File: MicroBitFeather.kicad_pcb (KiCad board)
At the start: 2 copper layers, 16 parts, among them J1 Feather_Long, J2 Barrel_Jack_MountingPin, J3 Feather_Short, J4 NeoPixels, J5 microbit_edge_connector, U1 74AHCT125, U2 MCP1702-3302E_TO92

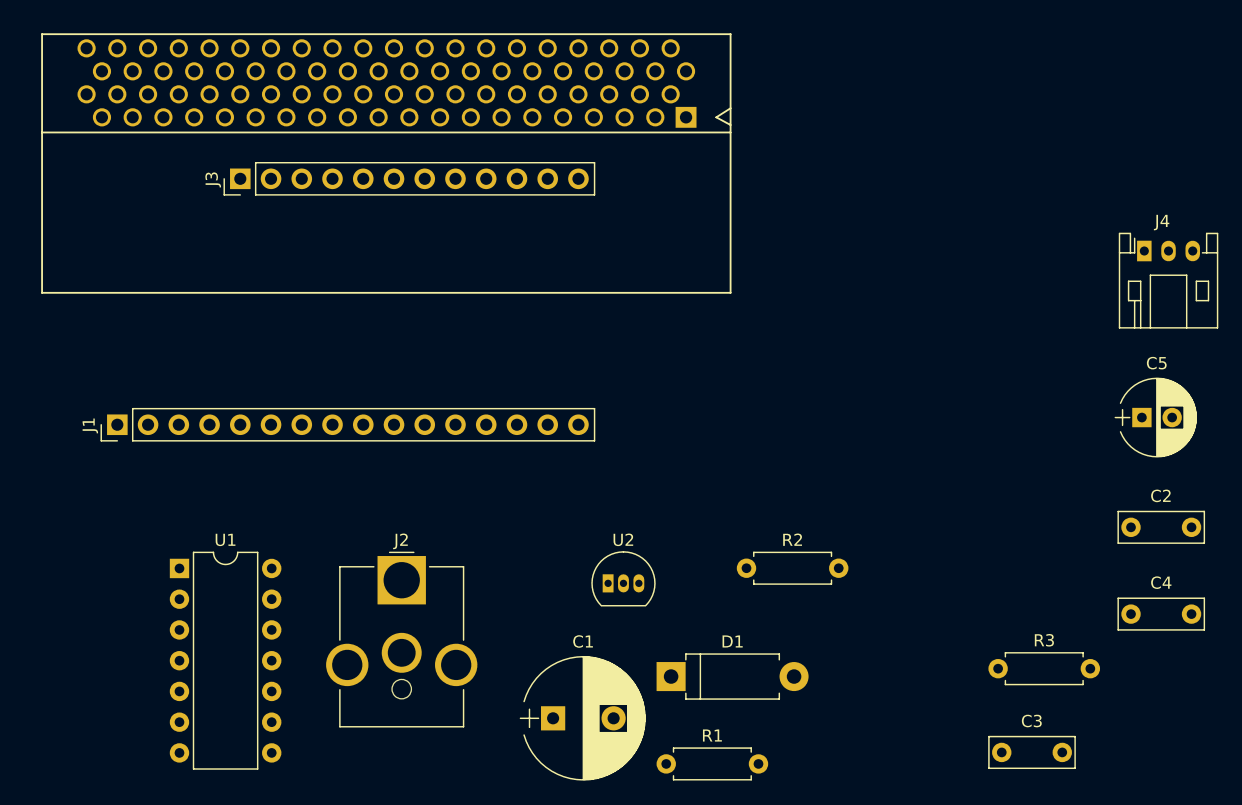
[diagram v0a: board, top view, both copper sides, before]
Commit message: Place footprints.
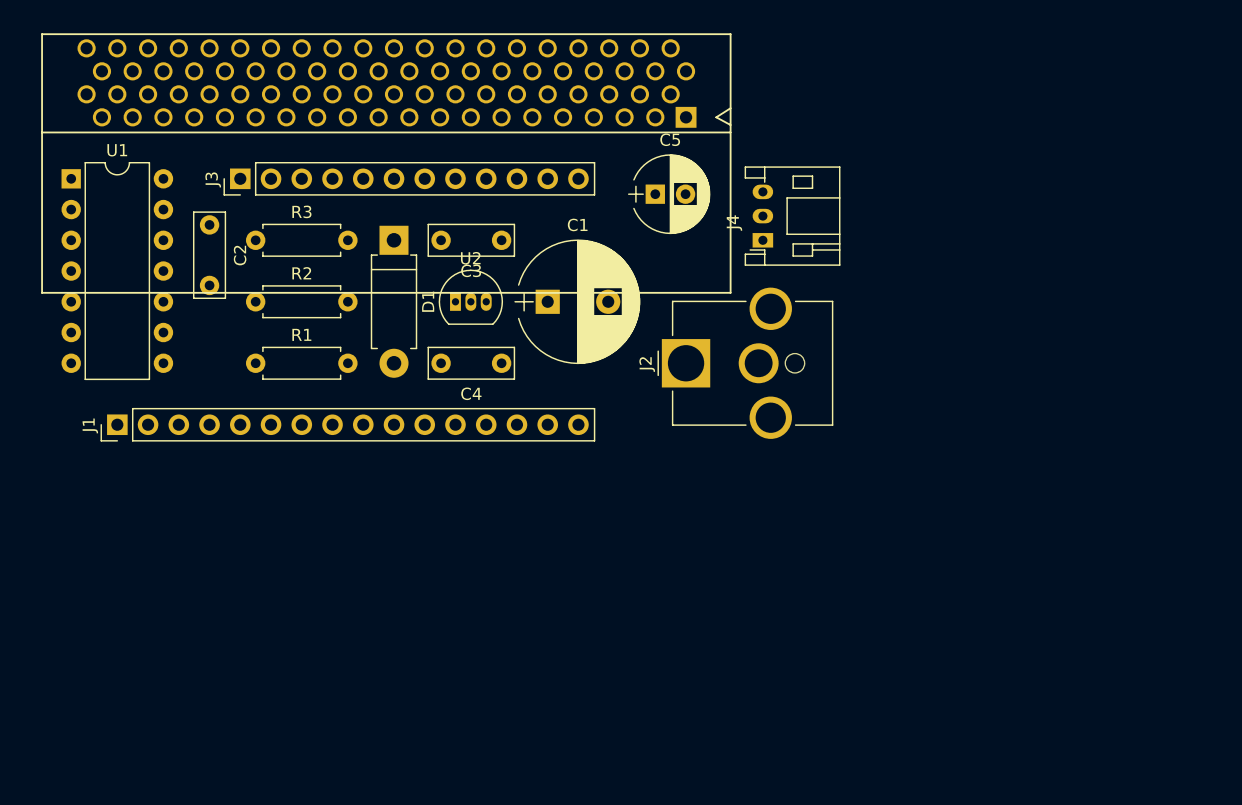
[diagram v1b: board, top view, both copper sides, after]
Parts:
- moved C2 80.1 mm to (133.3, 100.3), turned to 270 degrees
- moved R3 70.8 mm to (137.2, 101.6)
- moved C3 59.1 mm to (157.5, 101.6), turned to 180 degrees
- moved C4 56.0 mm to (157.5, 111.8), turned to 180 degrees
- moved R1 47.4 mm to (137.2, 111.8)
- moved R2 46.1 mm to (137.2, 106.7)
- moved C5 44.2 mm to (170.2, 97.8)
- moved D1 42.7 mm to (148.6, 101.6), turned to 270 degrees
- moved C1 34.4 mm to (161.3, 106.7)
- moved U1 33.4 mm to (121.9, 96.5)
- moved J4 31.5 mm to (179.1, 101.6), turned to 90 degrees
- moved J2 29.5 mm to (172.7, 111.8), turned to 90 degrees
- moved U2 26.5 mm to (153.7, 106.7)

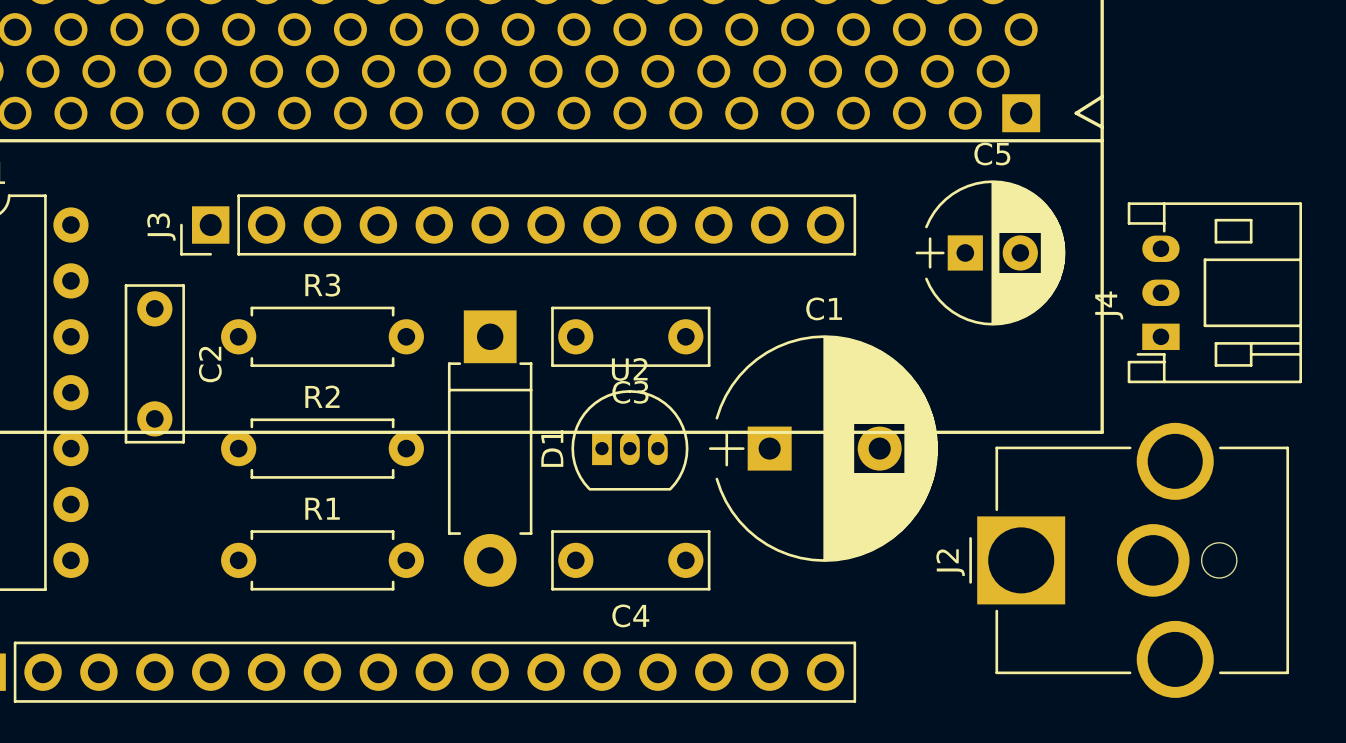
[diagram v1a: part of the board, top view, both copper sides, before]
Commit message: Tweaks to footprint placement.
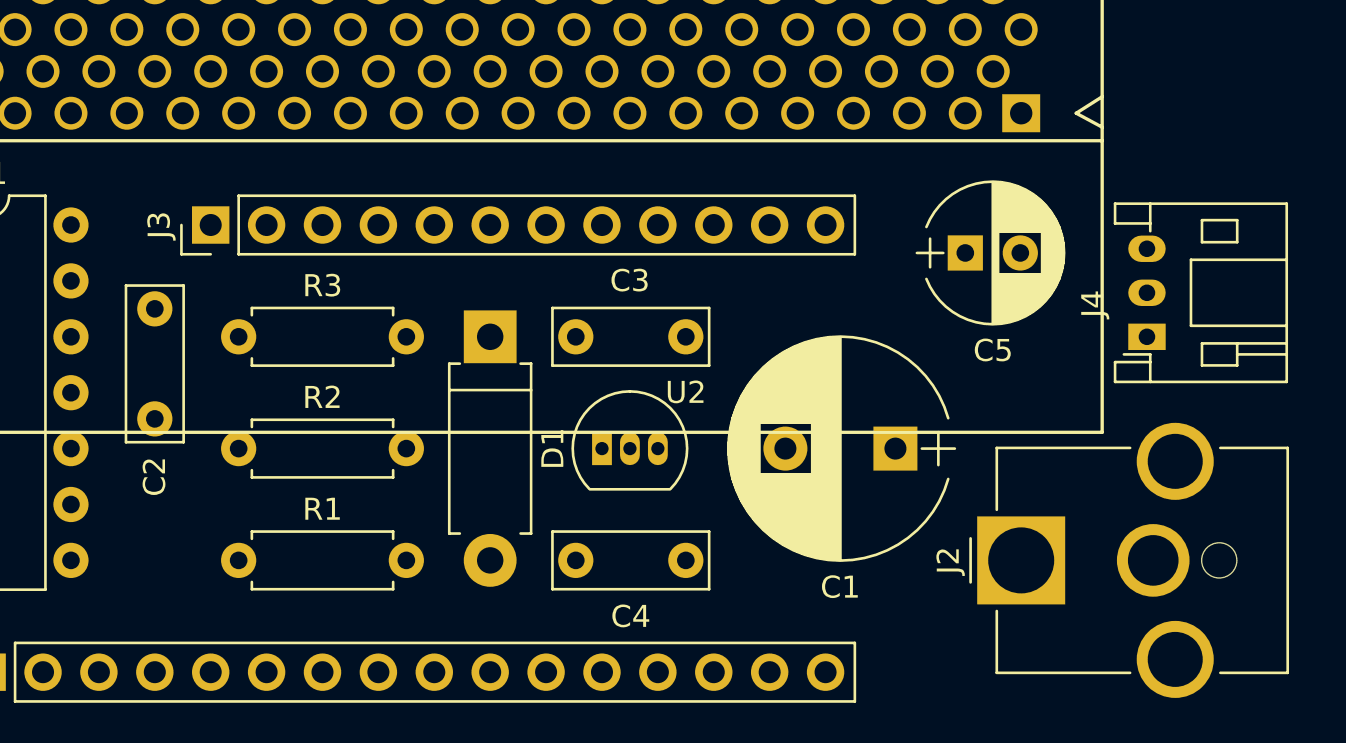
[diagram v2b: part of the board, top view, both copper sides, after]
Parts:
- moved C1 5.72 mm to (167.0, 106.7), turned to 180 degrees
- moved J4 0.63 mm to (178.4, 101.6)
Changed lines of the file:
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@@
   )
   (module Capacitors_THT:CP_Radial_D10.0mm_P5.00mm (layer F.Cu)
-    (at 161.29 106.68)
+    (at 167.005 106.68 180)
     (descr "CP, Radial series, Radial, pin pitch=5.00mm, , diameter=10mm, Electrolytic Capacitor")
     (tags "CP Radial series Radial pin pitch 5.00mm  diameter 10mm Electrolytic Capacitor")
-    (fp_text reference C1 (at 2.5 -6.31) (layer F.SilkS)
-      (effects (font (size 1 1) (thickness 0.15)))
-    )
-    (fp_text value 1000µF (at 2.5 6.31) (layer F.Fab)
+    (fp_text reference C1 (at 2.5 -6.31 180) (layer F.SilkS)
+      (effects (font (size 1 1) (thickness 0.15)))
+    )
+    (fp_text value 1000µF (at 2.5 6.31 180) (layer F.Fab)
       (effects (font (size 1 1) (thickness 0.15)))
     )
@@
     (fp_line (start 7.85 5.35) (end 7.85 -5.35) (layer F.CrtYd) (width 0.05))
     (fp_line (start 7.85 -5.35) (end -2.85 -5.35) (layer F.CrtYd) (width 0.05))
-    (fp_text user %R (at 2.5 0) (layer F.Fab)
-      (effects (font (size 1 1) (thickness 0.15)))
-    )
-    (pad 1 thru_hole rect (at 0 0) (size 2 2) (drill 1) (layers *.Cu *.Mask)
+    (fp_text user %R (at 2.5 0 180) (layer F.Fab)
+      (effects (font (size 1 1) (thickness 0.15)))
+    )
+    (pad 1 thru_hole rect (at 0 0 180) (size 2 2) (drill 1) (layers *.Cu *.Mask)
       (net 1 +5V))
-    (pad 2 thru_hole circle (at 5 0) (size 2 2) (drill 1) (layers *.Cu *.Mask)
+    (pad 2 thru_hole circle (at 5 0 180) (size 2 2) (drill 1) (layers *.Cu *.Mask)
       (net 2 GND))
     (model ${KISYS3DMOD}/Capacitors_THT.3dshapes/CP_Radial_D10.0mm_P5.00mm.wrl
@@
     (descr "C, Rect series, Radial, pin pitch=5.00mm, , length*width=7*2.5mm^2, Capacitor")
     (tags "C Rect series Radial pin pitch 5.00mm  length 7mm width 2.5mm Capacitor")
-    (fp_text reference C2 (at 2.5 -2.56 270) (layer F.SilkS)
+    (fp_text reference C2 (at 7.62 0 270) (layer F.SilkS)
       (effects (font (size 1 1) (thickness 0.15)))
     )
@@
     (descr "C, Rect series, Radial, pin pitch=5.00mm, , length*width=7*2.5mm^2, Capacitor")
     (tags "C Rect series Radial pin pitch 5.00mm  length 7mm width 2.5mm Capacitor")
-    (fp_text reference C3 (at 2.5 -2.56 180) (layer F.SilkS)
+    (fp_text reference C3 (at 2.54 2.54 180) (layer F.SilkS)
       (effects (font (size 1 1) (thickness 0.15)))
     )
@@
     (descr "CP, Radial series, Radial, pin pitch=2.50mm, , diameter=6.3mm, Electrolytic Capacitor")
     (tags "CP Radial series Radial pin pitch 2.50mm  diameter 6.3mm Electrolytic Capacitor")
-    (fp_text reference C5 (at 1.25 -4.46) (layer F.SilkS)
+    (fp_text reference C5 (at 1.27 4.445) (layer F.SilkS)
       (effects (font (size 1 1) (thickness 0.15)))
     )
@@
   )
   (module Connectors_JST:JST_PH_S3B-PH-K_03x2.00mm_Angled (layer F.Cu)
-    (at 179.07 101.6 90)
+    (at 178.435 101.6 90)
     (descr "JST PH series connector, S3B-PH-K, side entry type, through hole, Datasheet: http://www.jst-mfg.com/product/pdf/eng/ePH.pdf")
     (tags "connector jst ph")
@@
     (descr "TO-92 leads in-line, narrow, oval pads, drill 0.6mm (see NXP sot054_po.pdf)")
     (tags "to-92 sc-43 sc-43a sot54 PA33 transistor")
-    (fp_text reference U2 (at 1.27 -3.56) (layer F.SilkS)
-      (effects (font (size 1 1) (thickness 0.15)))
-    )
+    (fp_text reference U2 (at 3.81 -2.54) (layer F.SilkS)
+      (effects (font (size 1 1) (thickness 0.15)))
+    )

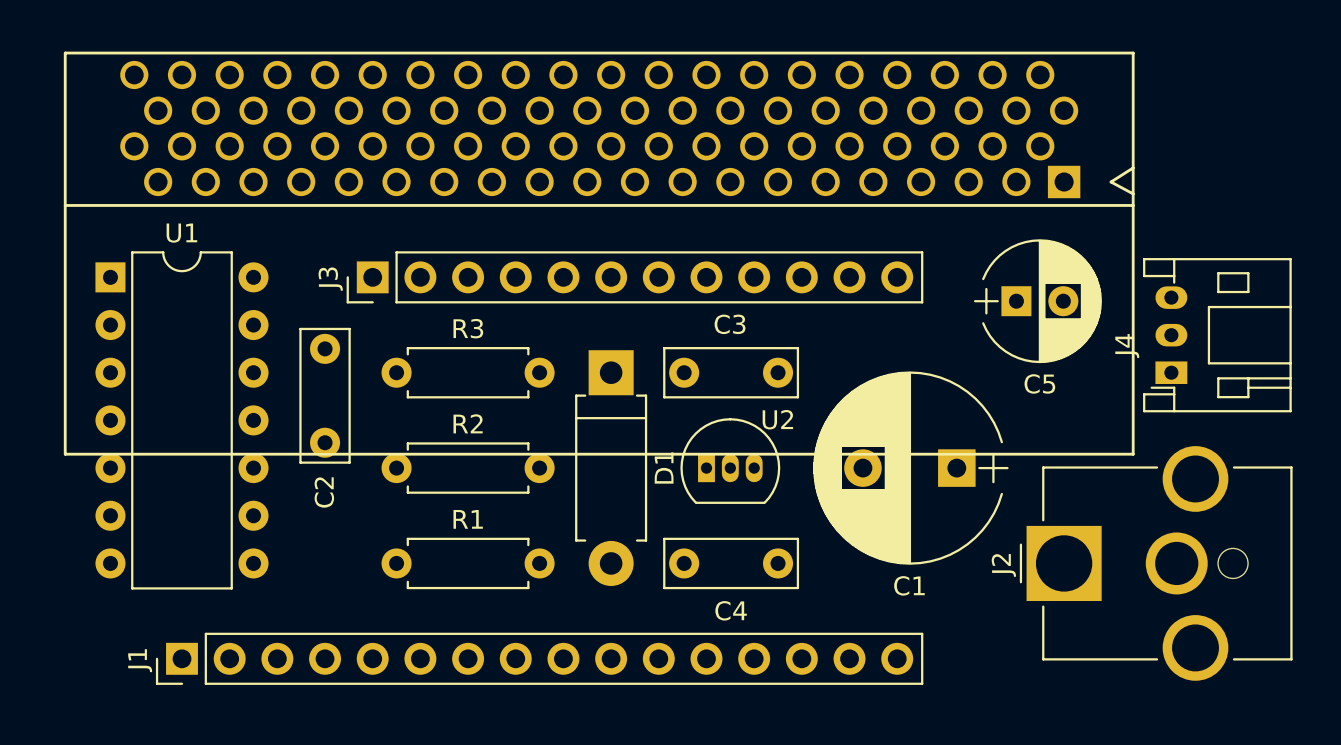
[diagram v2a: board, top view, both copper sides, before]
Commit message: Rounded corners for board outline.
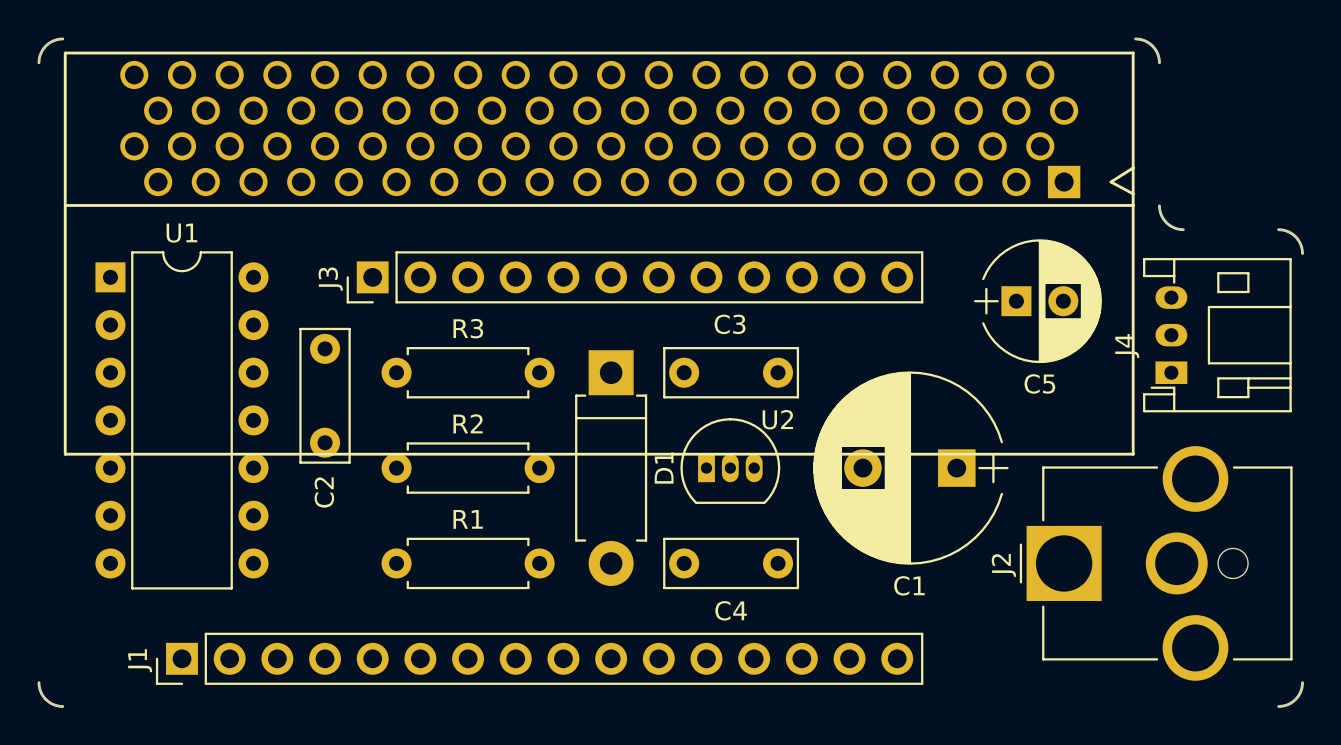
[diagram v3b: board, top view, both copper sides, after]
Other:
- board outline added: 67.3 x 35.6 mm
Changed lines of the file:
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@@
     (area 115.424999 71.584999 217.260002 148.48)
     (thickness 1.6)
-    (drawings 0)
+    (drawings 6)
     (tracks 0)
     (zones 0)
@@
     )
   )
+  (gr_arc (start 176.53 85.09) (end 176.53 83.82) (angle 90) (layer Edge.Cuts) (width 0.15))
+  (gr_arc (start 179.07 92.71) (end 179.07 93.98) (angle 90) (layer Edge.Cuts) (width 0.15))
+  (gr_arc (start 184.15 95.25) (end 184.15 93.98) (angle 90) (layer Edge.Cuts) (width 0.15))
+  (gr_arc (start 184.15 118.11) (end 185.42 118.11) (angle 90) (layer Edge.Cuts) (width 0.15))
+  (gr_arc (start 119.38 118.11) (end 119.38 119.38) (angle 90) (layer Edge.Cuts) (width 0.15))
+  (gr_arc (start 119.38 85.09) (end 118.11 85.09) (angle 90) (layer Edge.Cuts) (width 0.15))
 )
